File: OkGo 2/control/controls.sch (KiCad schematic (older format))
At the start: 28 parts

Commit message: Lots of footprinting.
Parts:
- gave numbers to parts that had none: 28

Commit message: Finished footprinting control, #7
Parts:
- removed Q201, Q202, Q203, Q204: BSS138BK, symbol Q_NMOS_DGS
- added Q201, Q202, Q203, Q204: BSS138BK, Housings_SOT-23_SOT-143_TSOT-6:SOT-23, symbol Q_NMOS_GSD
- P201, P203, P205, P207: footprint (none) -> common:JST-PA-4; Farnell 1830737 -> 1830749
- R205, R206, R211, R212: Farnell 2331783 -> 2331823

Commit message: Non-handsoldering footprints, fixes #17
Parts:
- R201, R202, R203, R204, R205, R206, R207, R208, R209, R210, R211, R212: footprint Resistors_SMD:R_0805_HandSoldering -> Resistors_SMD:R_0805
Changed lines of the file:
@@
 F 0 "R203" V 1850 2500 50  0000 C CNN
 F 1 "180R" V 1650 2500 50  0000 C CNN
-F 2 "Resistors_SMD:R_0805_HandSoldering" V 1680 2500 30  0001 C CNN
+F 2 "Resistors_SMD:R_0805" V 1680 2500 30  0001 C CNN
 F 3 "" H 1750 2500 30  0000 C CNN
 F 4 "2331786" H 1750 2500 60  0001 C CNN "Farnell"
@@
 F 0 "R205" V 2050 2700 50  0000 C CNN
 F 1 "100k" V 1850 2650 50  0000 C CNN
-F 2 "Resistors_SMD:R_0805_HandSoldering" V 1880 2700 30  0001 C CNN
+F 2 "Resistors_SMD:R_0805" V 1880 2700 30  0001 C CNN
 F 3 "" H 1950 2700 30  0000 C CNN
 F 4 "2331823" H 1950 2700 60  0001 C CNN "Farnell"
@@
 F 0 "R201" V 3050 1750 50  0000 C CNN
 F 1 "10k" V 2850 1750 50  0000 C CNN
-F 2 "Resistors_SMD:R_0805_HandSoldering" V 2880 1750 30  0001 C CNN
+F 2 "Resistors_SMD:R_0805" V 2880 1750 30  0001 C CNN
 F 3 "" H 2950 1750 30  0000 C CNN
 F 4 "2331808" H 2950 1750 60  0001 C CNN "Farnell"
@@
 F 0 "R209" V 1850 5300 50  0000 C CNN
 F 1 "180R" V 1650 5300 50  0000 C CNN
-F 2 "Resistors_SMD:R_0805_HandSoldering" V 1680 5300 30  0001 C CNN
+F 2 "Resistors_SMD:R_0805" V 1680 5300 30  0001 C CNN
 F 3 "" H 1750 5300 30  0000 C CNN
 F 4 "2331786" H 1750 5300 60  0001 C CNN "Farnell"
@@
 F 0 "R211" V 2050 5500 50  0000 C CNN
 F 1 "100k" V 1850 5450 50  0000 C CNN
-F 2 "Resistors_SMD:R_0805_HandSoldering" V 1880 5500 30  0001 C CNN
+F 2 "Resistors_SMD:R_0805" V 1880 5500 30  0001 C CNN
 F 3 "" H 1950 5500 30  0000 C CNN
 F 4 "2331823" H 1950 5500 60  0001 C CNN "Farnell"
@@
 F 0 "R207" V 3050 4550 50  0000 C CNN
 F 1 "10k" V 2850 4550 50  0000 C CNN
-F 2 "Resistors_SMD:R_0805_HandSoldering" V 2880 4550 30  0001 C CNN
+F 2 "Resistors_SMD:R_0805" V 2880 4550 30  0001 C CNN
 F 3 "" H 2950 4550 30  0000 C CNN
 F 4 "2331808" H 2950 4550 60  0001 C CNN "Farnell"
@@
 F 0 "R204" V 6350 2500 50  0000 C CNN
 F 1 "180R" V 6150 2500 50  0000 C CNN
-F 2 "Resistors_SMD:R_0805_HandSoldering" V 6180 2500 30  0001 C CNN
+F 2 "Resistors_SMD:R_0805" V 6180 2500 30  0001 C CNN
 F 3 "" H 6250 2500 30  0000 C CNN
 F 4 "2331786" H 6250 2500 60  0001 C CNN "Farnell"
@@
 F 0 "R206" V 6550 2700 50  0000 C CNN
 F 1 "100k" V 6350 2650 50  0000 C CNN
-F 2 "Resistors_SMD:R_0805_HandSoldering" V 6380 2700 30  0001 C CNN
+F 2 "Resistors_SMD:R_0805" V 6380 2700 30  0001 C CNN
 F 3 "" H 6450 2700 30  0000 C CNN
 F 4 "2331823" H 6450 2700 60  0001 C CNN "Farnell"
@@
 F 0 "R202" V 7550 1750 50  0000 C CNN
 F 1 "10k" V 7350 1750 50  0000 C CNN
-F 2 "Resistors_SMD:R_0805_HandSoldering" V 7380 1750 30  0001 C CNN
+F 2 "Resistors_SMD:R_0805" V 7380 1750 30  0001 C CNN
 F 3 "" H 7450 1750 30  0000 C CNN
 F 4 "2331808" H 7450 1750 60  0001 C CNN "Farnell"
@@
 F 0 "R210" V 6450 5300 50  0000 C CNN
 F 1 "180R" V 6250 5300 50  0000 C CNN
-F 2 "Resistors_SMD:R_0805_HandSoldering" V 6280 5300 30  0001 C CNN
+F 2 "Resistors_SMD:R_0805" V 6280 5300 30  0001 C CNN
 F 3 "" H 6350 5300 30  0000 C CNN
 F 4 "2331786" H 6350 5300 60  0001 C CNN "Farnell"
@@
 F 0 "R212" V 6650 5500 50  0000 C CNN
 F 1 "100k" V 6450 5450 50  0000 C CNN
-F 2 "Resistors_SMD:R_0805_HandSoldering" V 6480 5500 30  0001 C CNN
+F 2 "Resistors_SMD:R_0805" V 6480 5500 30  0001 C CNN
 F 3 "" H 6550 5500 30  0000 C CNN
 F 4 "2331823" H 6550 5500 60  0001 C CNN "Farnell"
@@
 F 0 "R208" V 7650 4550 50  0000 C CNN
 F 1 "10k" V 7450 4550 50  0000 C CNN
-F 2 "Resistors_SMD:R_0805_HandSoldering" V 7480 4550 30  0001 C CNN
+F 2 "Resistors_SMD:R_0805" V 7480 4550 30  0001 C CNN
 F 3 "" H 7550 4550 30  0000 C CNN
 F 4 "2331808" H 7550 4550 60  0001 C CNN "Farnell"

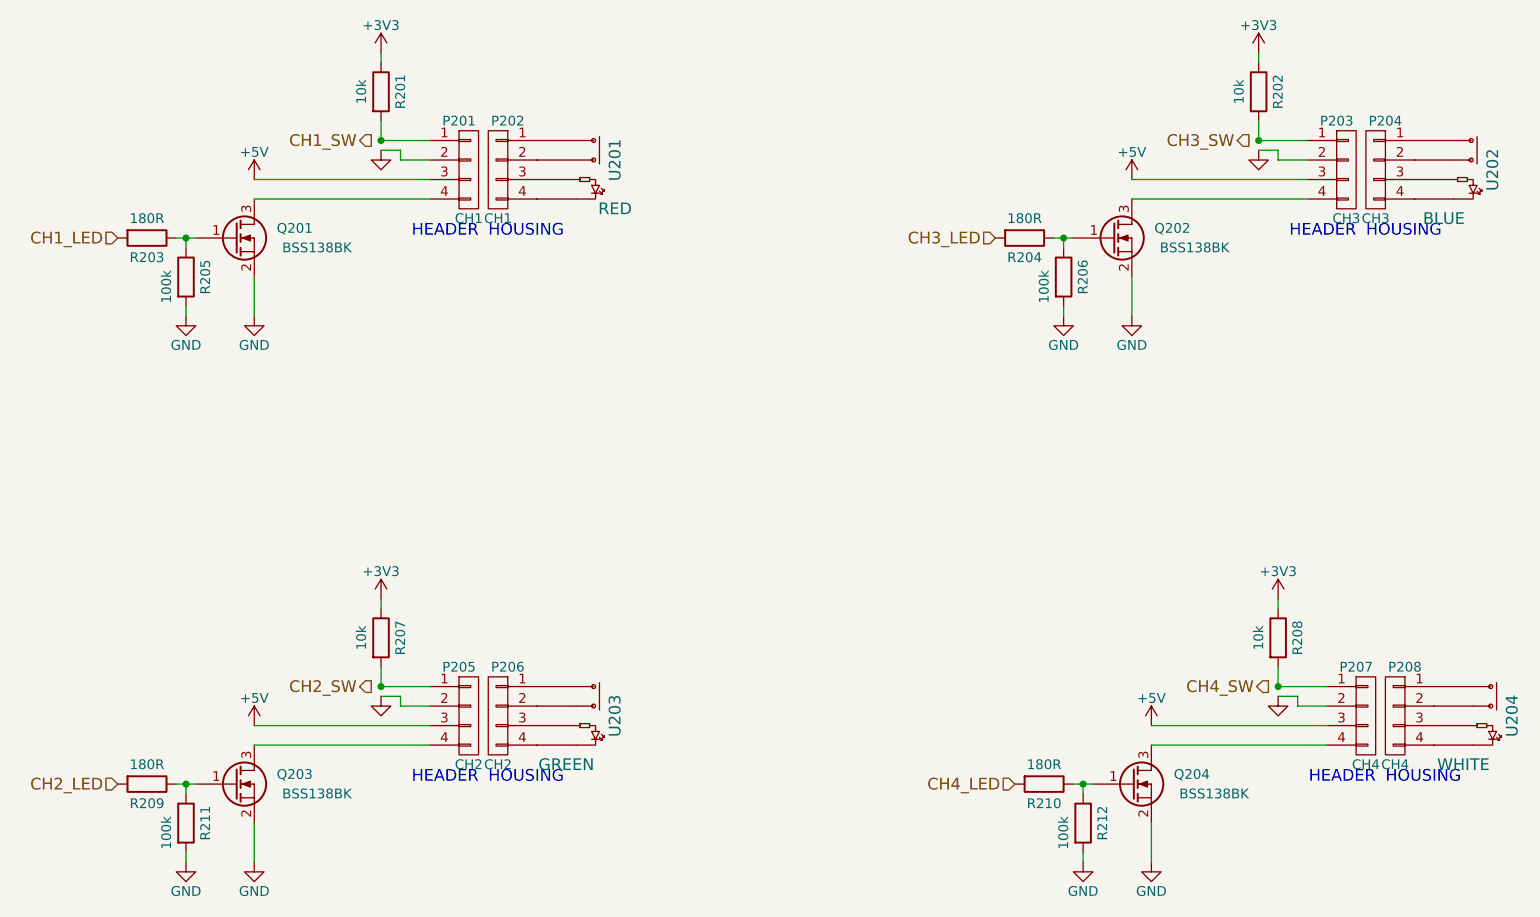
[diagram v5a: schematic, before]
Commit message: 4-bit LCD, pulldowns, 2-pin bicolour ARM LED
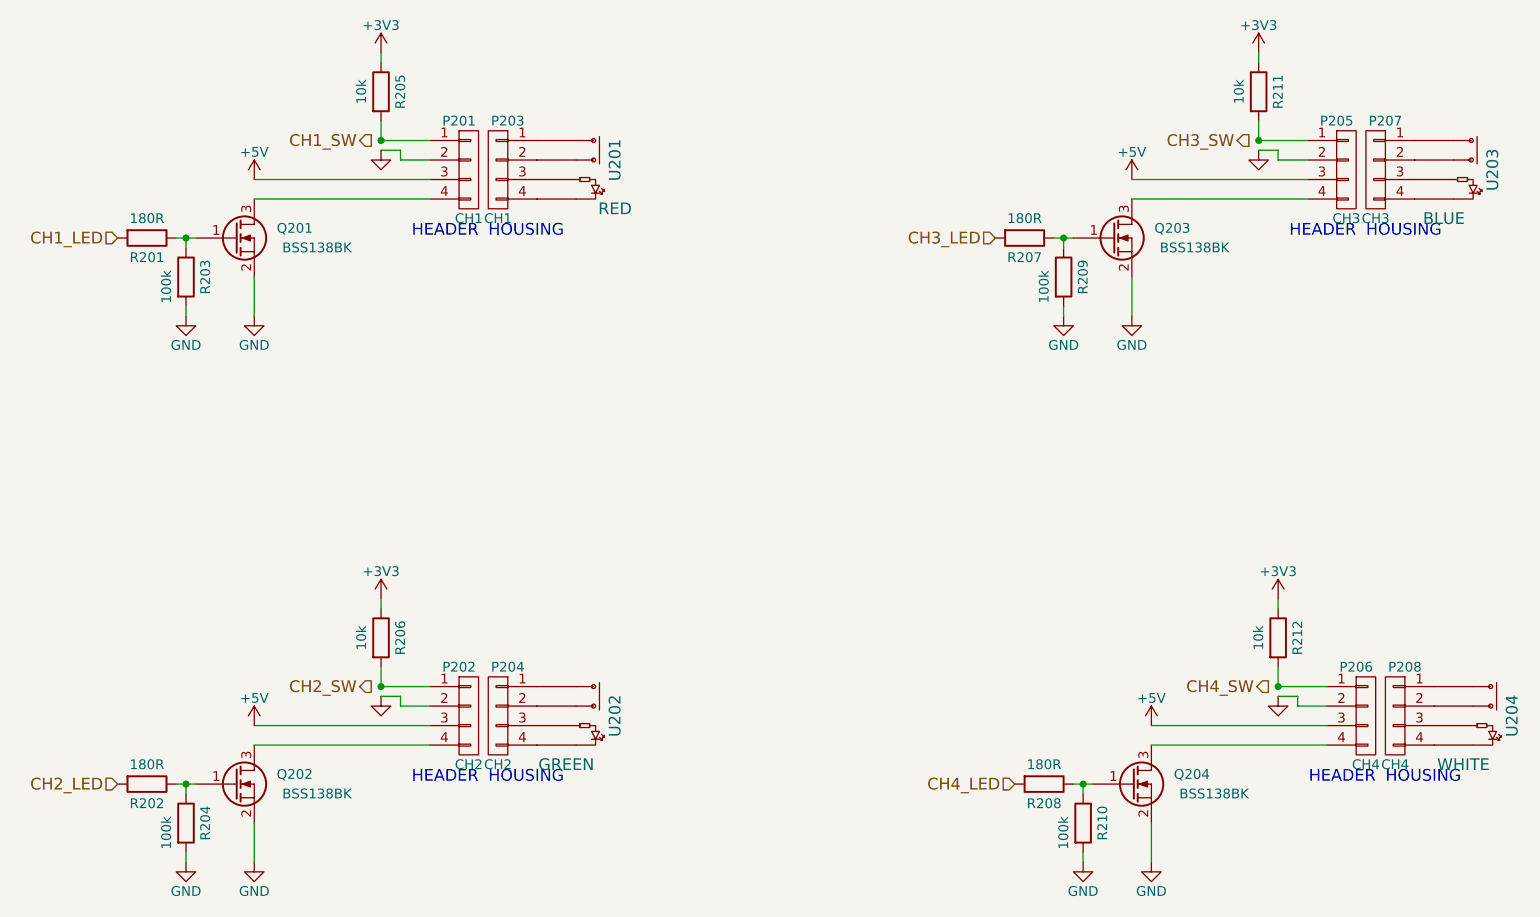
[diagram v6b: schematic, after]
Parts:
- renumbered P205 to P202, P202 to P203, P206 to P204, P203 to P205, P207 to P206, P204 to P207, Q203 to Q202, Q202 to Q203, R203 to R201, R209 to R202, R205 to R203, R211 to R204, R201 to R205, R207 to R206, R204 to R207, R210 to R208, R206 to R209, R212 to R210, R202 to R211, R208 to R212, U203 to U202, U202 to U203
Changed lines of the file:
@@
 LIBS:push_illum_straight
 LIBS:mej2s0305sc
+LIBS:led_bicolour
 LIBS:control-cache
 EELAYER 25 0
@@
 $EndComp
 $Comp
-L R R203
+L R R201
 U 1 1 559EE1D6
 P 1750 2500
-F 0 "R203" V 1850 2500 50  0000 C CNN
+F 0 "R201" V 1850 2500 50  0000 C CNN
 F 1 "180R" V 1650 2500 50  0000 C CNN
 F 2 "Resistors_SMD:R_0805" V 1680 2500 30  0001 C CNN
@@
 $EndComp
 $Comp
-L R R205
+L R R203
 U 1 1 559EE1DD
 P 1950 2700
-F 0 "R205" V 2050 2700 50  0000 C CNN
+F 0 "R203" V 2050 2700 50  0000 C CNN
 F 1 "100k" V 1850 2650 50  0000 C CNN
 F 2 "Resistors_SMD:R_0805" V 1880 2700 30  0001 C CNN
@@
 $EndComp
 $Comp
-L R R201
+L R R205
 U 1 1 559EE1FB
 P 2950 1750
-F 0 "R201" V 3050 1750 50  0000 C CNN
+F 0 "R205" V 3050 1750 50  0000 C CNN
 F 1 "10k" V 2850 1750 50  0000 C CNN
 F 2 "Resistors_SMD:R_0805" V 2880 1750 30  0001 C CNN
@@
 CH1_SW
 $Comp
-L CONN_01X04 P202
+L CONN_01X04 P203
 U 1 1 559F1DAA
 P 3550 2150
-F 0 "P202" H 3500 2400 50  0000 C CNN
+F 0 "P203" H 3500 2400 50  0000 C CNN
 F 1 "CH1" H 3550 1900 50  0000 C CNN
 F 2 "" H 3550 2150 60  0000 C CNN
@@
 	2300 2300 3200 2300
 $Comp
-L CONN_01X04 P205
+L CONN_01X04 P202
 U 1 1 559F3714
 P 3400 4950
-F 0 "P205" H 3350 5200 50  0000 C CNN
+F 0 "P202" H 3350 5200 50  0000 C CNN
 F 1 "CH2" H 3400 4700 50  0000 C CNN
 F 2 "common:JST-PA-4" H 3400 4950 60  0001 C CNN
@@
 $EndComp
 $Comp
-L R R209
+L R R202
 U 1 1 559F3722
 P 1750 5300
-F 0 "R209" V 1850 5300 50  0000 C CNN
+F 0 "R202" V 1850 5300 50  0000 C CNN
 F 1 "180R" V 1650 5300 50  0000 C CNN
 F 2 "Resistors_SMD:R_0805" V 1680 5300 30  0001 C CNN
@@
 $EndComp
 $Comp
-L R R211
+L R R204
 U 1 1 559F3729
 P 1950 5500
-F 0 "R211" V 2050 5500 50  0000 C CNN
+F 0 "R204" V 2050 5500 50  0000 C CNN
 F 1 "100k" V 1850 5450 50  0000 C CNN
 F 2 "Resistors_SMD:R_0805" V 1880 5500 30  0001 C CNN
@@
 $EndComp
 $Comp
-L R R207
+L R R206
 U 1 1 559F373C
 P 2950 4550
-F 0 "R207" V 3050 4550 50  0000 C CNN
+F 0 "R206" V 3050 4550 50  0000 C CNN
 F 1 "10k" V 2850 4550 50  0000 C CNN
 F 2 "Resistors_SMD:R_0805" V 2880 4550 30  0001 C CNN
@@
 CH2_SW
 $Comp
-L CONN_01X04 P206
+L CONN_01X04 P204
 U 1 1 559F3750
 P 3550 4950
-F 0 "P206" H 3500 5200 50  0000 C CNN
+F 0 "P204" H 3500 5200 50  0000 C CNN
 F 1 "CH2" H 3550 4700 50  0000 C CNN
 F 2 "" H 3550 4950 60  0000 C CNN
@@
 $EndComp
 $Comp
-L PUSH_ILLUM U203
+L PUSH_ILLUM U202
 U 1 1 559F3756
 P 4150 4700
-F 0 "U203" V 4150 4450 60  0000 C CNN
+F 0 "U202" V 4150 4450 60  0000 C CNN
 F 1 "GREEN" H 3900 4200 60  0000 C CNN
 F 2 "" H 4150 4700 60  0000 C CNN
@@
 	2300 5100 3200 5100
 $Comp
-L CONN_01X04 P203
+L CONN_01X04 P205
 U 1 1 559F3AAA
 P 7900 2150
-F 0 "P203" H 7850 2400 50  0000 C CNN
+F 0 "P205" H 7850 2400 50  0000 C CNN
 F 1 "CH3" H 7900 1900 50  0000 C CNN
 F 2 "common:JST-PA-4" H 7900 2150 60  0001 C CNN
@@
 $EndComp
 $Comp
-L R R204
+L R R207
 U 1 1 559F3AB8
 P 6250 2500
-F 0 "R204" V 6350 2500 50  0000 C CNN
+F 0 "R207" V 6350 2500 50  0000 C CNN
 F 1 "180R" V 6150 2500 50  0000 C CNN
 F 2 "Resistors_SMD:R_0805" V 6180 2500 30  0001 C CNN
@@
 $EndComp
 $Comp
-L R R206
+L R R209
 U 1 1 559F3ABF
 P 6450 2700
-F 0 "R206" V 6550 2700 50  0000 C CNN
+F 0 "R209" V 6550 2700 50  0000 C CNN
 F 1 "100k" V 6350 2650 50  0000 C CNN
 F 2 "Resistors_SMD:R_0805" V 6380 2700 30  0001 C CNN
@@
 $EndComp
 $Comp
-L R R202
+L R R211
 U 1 1 559F3AD2
 P 7450 1750
-F 0 "R202" V 7550 1750 50  0000 C CNN
+F 0 "R211" V 7550 1750 50  0000 C CNN
 F 1 "10k" V 7350 1750 50  0000 C CNN
 F 2 "Resistors_SMD:R_0805" V 7380 1750 30  0001 C CNN
@@
 CH3_SW
 $Comp
-L CONN_01X04 P204
+L CONN_01X04 P207
 U 1 1 559F3AE6
 P 8050 2150
-F 0 "P204" H 8000 2400 50  0000 C CNN
+F 0 "P207" H 8000 2400 50  0000 C CNN
 F 1 "CH3" H 8050 1900 50  0000 C CNN
 F 2 "" H 8050 2150 60  0000 C CNN
@@
 $EndComp
 $Comp
-L PUSH_ILLUM U202
+L PUSH_ILLUM U203
 U 1 1 559F3AEC
 P 8650 1900
-F 0 "U202" V 8650 1650 60  0000 C CNN
+F 0 "U203" V 8650 1650 60  0000 C CNN
 F 1 "BLUE" H 8400 1400 60  0000 C CNN
 F 2 "" H 8650 1900 60  0000 C CNN
@@
 	6800 2300 7700 2300
 $Comp
-L CONN_01X04 P207
+L CONN_01X04 P206
 U 1 1 559F3DDE
 P 8000 4950
-F 0 "P207" H 7950 5200 50  0000 C CNN
+F 0 "P206" H 7950 5200 50  0000 C CNN
 F 1 "CH4" H 8000 4700 50  0000 C CNN
 F 2 "common:JST-PA-4" H 8000 4950 60  0001 C CNN
@@
 $EndComp
 $Comp
-L R R210
+L R R208
 U 1 1 559F3DEC
 P 6350 5300
-F 0 "R210" V 6450 5300 50  0000 C CNN
+F 0 "R208" V 6450 5300 50  0000 C CNN
 F 1 "180R" V 6250 5300 50  0000 C CNN
 F 2 "Resistors_SMD:R_0805" V 6280 5300 30  0001 C CNN
@@
 $EndComp
 $Comp
-L R R212
+L R R210
 U 1 1 559F3DF3
 P 6550 5500
-F 0 "R212" V 6650 5500 50  0000 C CNN
+F 0 "R210" V 6650 5500 50  0000 C CNN
 F 1 "100k" V 6450 5450 50  0000 C CNN
 F 2 "Resistors_SMD:R_0805" V 6480 5500 30  0001 C CNN
@@
 $EndComp
 $Comp
-L R R208
+L R R212
 U 1 1 559F3E06
 P 7550 4550
-F 0 "R208" V 7650 4550 50  0000 C CNN
+F 0 "R212" V 7650 4550 50  0000 C CNN
 F 1 "10k" V 7450 4550 50  0000 C CNN
 F 2 "Resistors_SMD:R_0805" V 7480 4550 30  0001 C CNN
@@
 $EndComp
 $Comp
-L Q_NMOS_GSD Q203
+L Q_NMOS_GSD Q202
 U 1 1 55AA6B4A
 P 2200 5300
-F 0 "Q203" H 2600 5350 50  0000 R CNN
+F 0 "Q202" H 2600 5350 50  0000 R CNN
 F 1 "BSS138BK" H 2800 5250 50  0000 R CNN
 F 2 "Housings_SOT-23_SOT-143_TSOT-6:SOT-23" H 2400 5400 29  0001 C CNN
@@
 $EndComp
 $Comp
-L Q_NMOS_GSD Q202
+L Q_NMOS_GSD Q203
 U 1 1 55AA6D6C
 P 6700 2500
-F 0 "Q202" H 7100 2550 50  0000 R CNN
+F 0 "Q203" H 7100 2550 50  0000 R CNN
 F 1 "BSS138BK" H 7300 2450 50  0000 R CNN
 F 2 "Housings_SOT-23_SOT-143_TSOT-6:SOT-23" H 6900 2600 29  0001 C CNN

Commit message: Finished demo-route of control
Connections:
- net CH1_SW: now also P201.1 (P1), R205.2
- net CH2_SW: now also P202.1 (P1), R206.2
- net CH3_SW: now also P205.1 (P1), R211.2
- net CH4_SW: now also P206.1 (P1), R212.2
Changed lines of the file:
@@
 $EndComp
 Wire Wire Line
-	2950 2000 3200 2000
+	2900 2000 3200 2000
 Wire Wire Line
 	2300 2200 3200 2200
@@
 $EndComp
 Wire Wire Line
-	2950 4800 3200 4800
+	2900 4800 3200 4800
 Wire Wire Line
 	2300 5000 3200 5000
@@
 $EndComp
 Wire Wire Line
-	7450 2000 7700 2000
+	7400 2000 7700 2000
 Wire Wire Line
 	6800 2200 7700 2200
@@
 $EndComp
 Wire Wire Line
-	7550 4800 7800 4800
+	7500 4800 7800 4800
 Wire Wire Line
 	6900 5000 7800 5000
